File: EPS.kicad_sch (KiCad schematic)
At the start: 30 parts, among them SW101 Deploy_1, SW102 Deploy_2

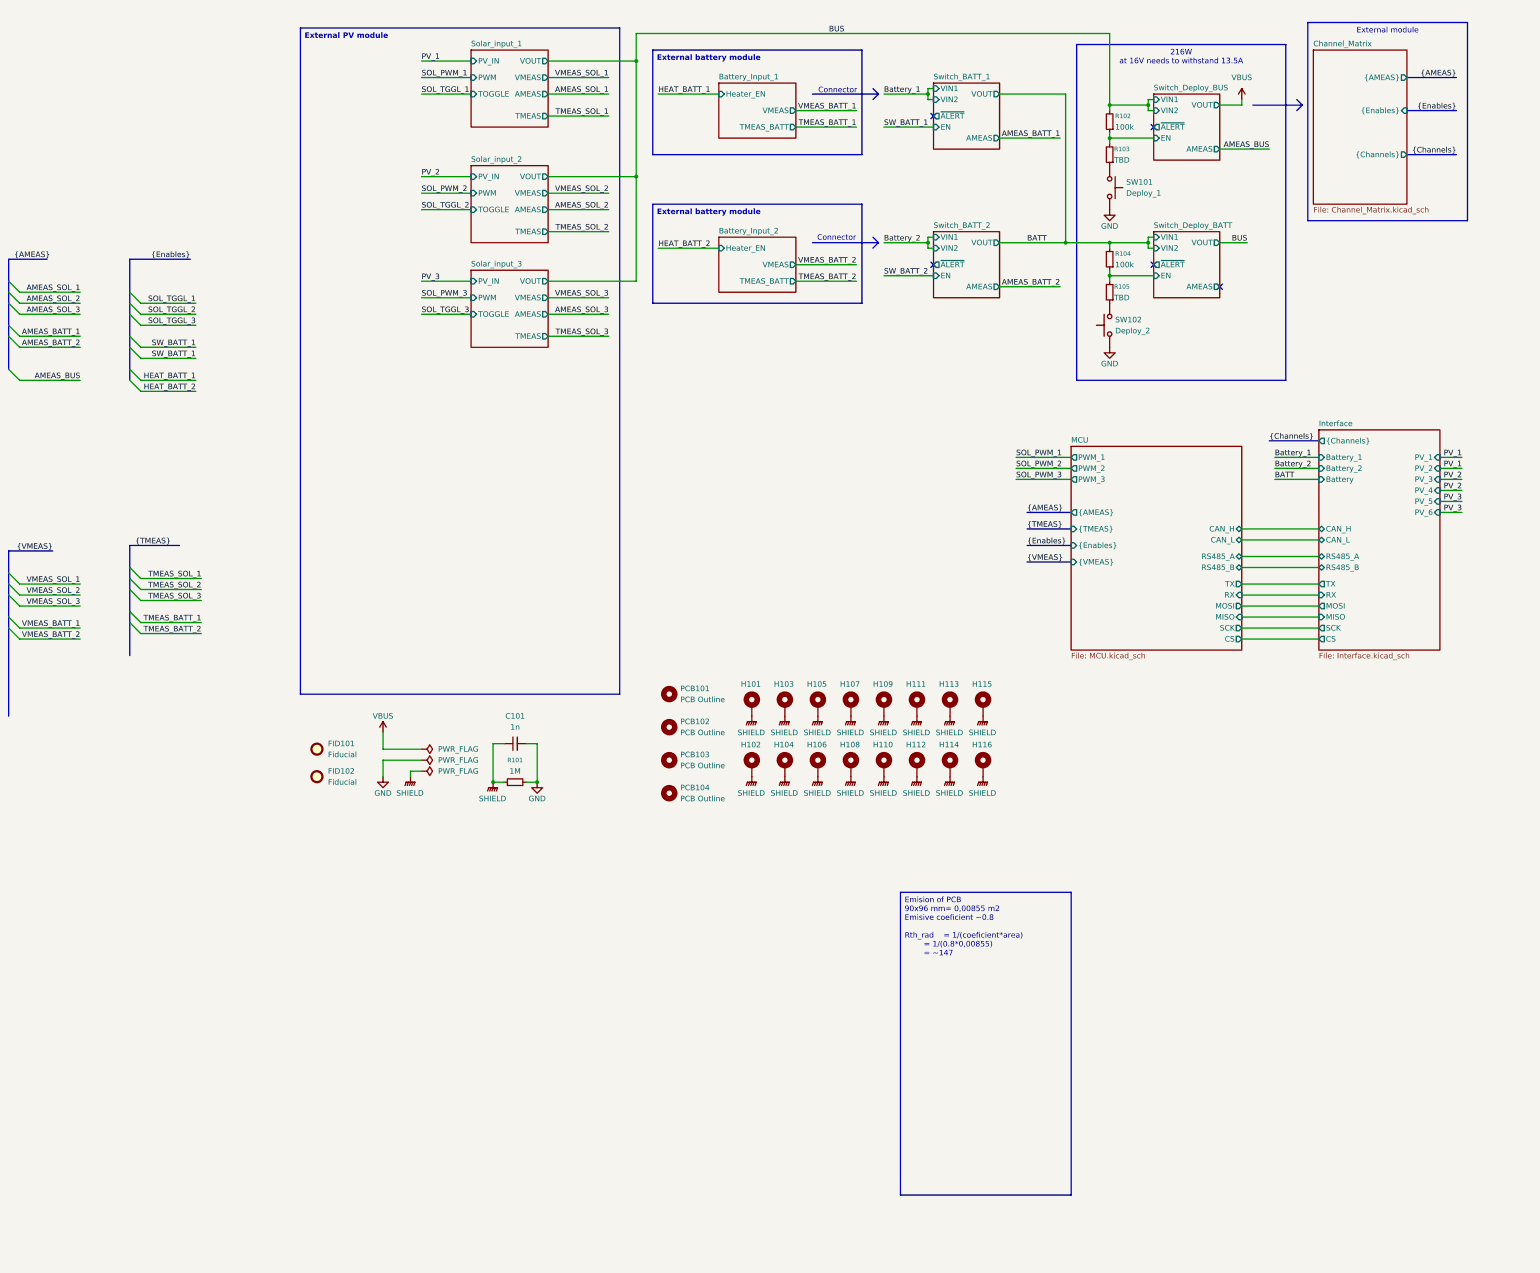
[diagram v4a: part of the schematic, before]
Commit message: connected CAN driver, added 3 solar inputs
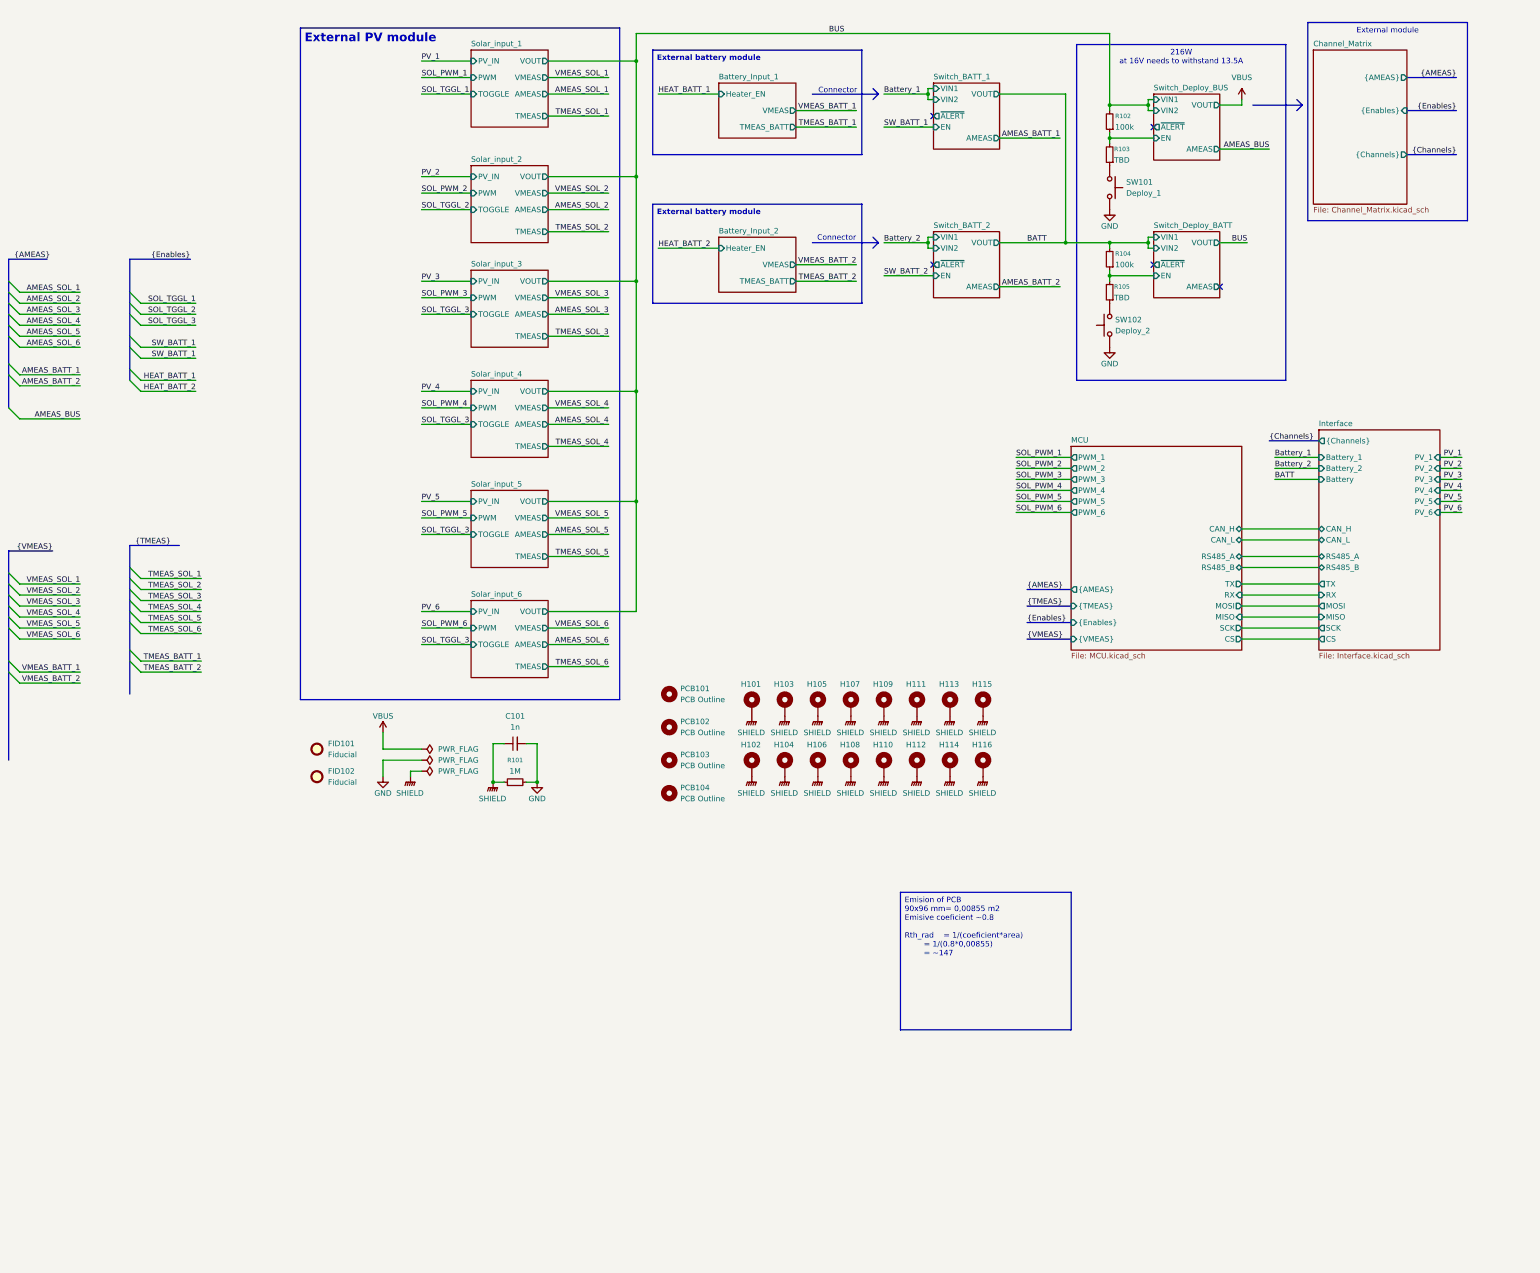
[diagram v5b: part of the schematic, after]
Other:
- added sheet Solar_input_4 (Solar_Cell_Input.kicad_sch)
- added sheet Solar_input_5 (Solar_Cell_Input.kicad_sch)
- added sheet Solar_input_6 (Solar_Cell_Input.kicad_sch)
- sheet MCU ports: added PWM_4, PWM_5, PWM_6; removed none

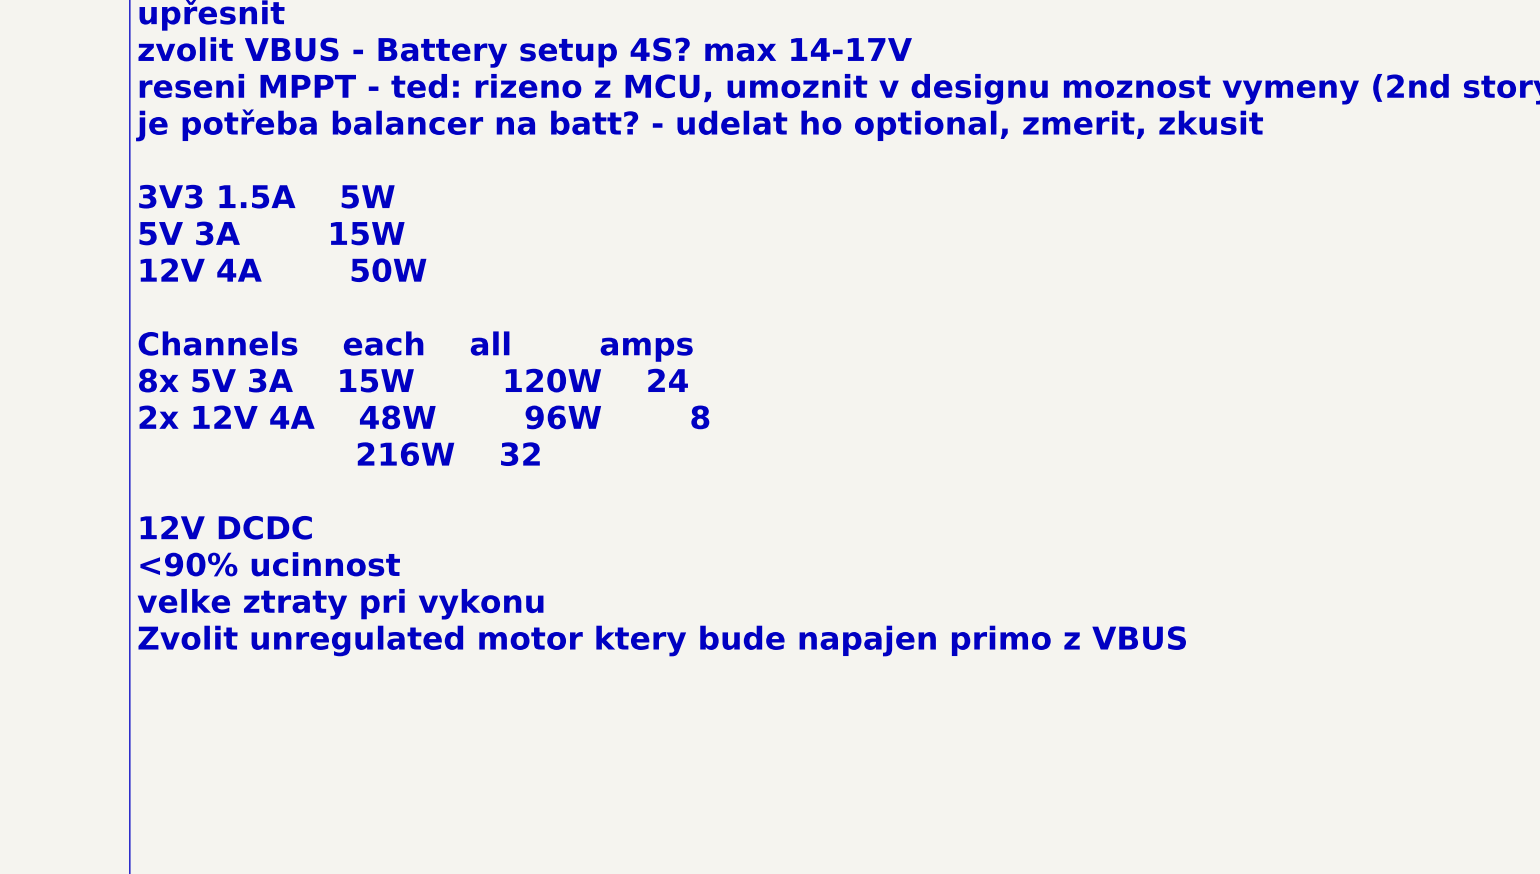
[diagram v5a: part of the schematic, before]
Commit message: added possible solutions for mppt
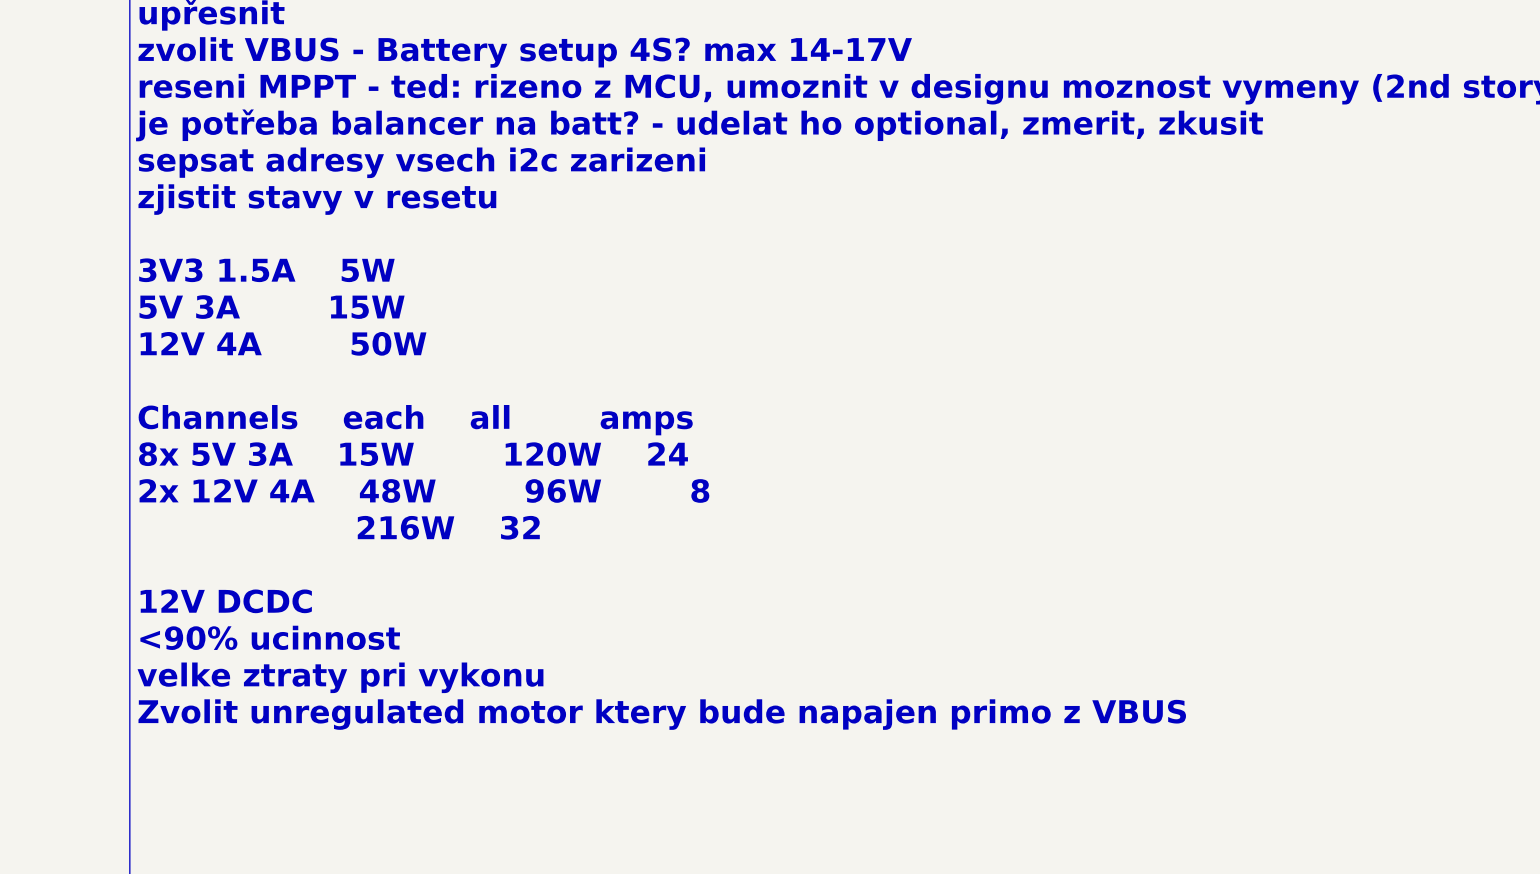
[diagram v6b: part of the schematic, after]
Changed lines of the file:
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@@
 		)
 	)
-	(text_box "upřesnit\nzvolit VBUS - Battery setup 4S? max 14-17V\nreseni MPPT - ted: rizeno z MCU, umoznit v designu moznost vymeny (2nd story nebo pajeny pcb modul)\nje potřeba balancer na batt? - udelat ho optional, zmerit, zkusit\n\n3V3 1.5A	5W\n5V 3A		15W\n12V 4A		50W\n\nChannels	each	all		amps\n8x 5V 3A	15W		120W	24\n2x 12V 4A	48W		96W		8\n					216W	32\n\n12V DCDC \n<90% ucinnost \nvelke ztraty pri vykonu\nZvolit unregulated motor ktery bude napajen primo z VBUS"
+	(text_box "upřesnit\nzvolit VBUS - Battery setup 4S? max 14-17V\nreseni MPPT - ted: rizeno z MCU, umoznit v designu moznost vymeny (2nd story nebo pajeny pcb modul)\nje potřeba balancer na batt? - udelat ho optional, zmerit, zkusit\nsepsat adresy vsech i2c zarizeni\nzjistit stavy v resetu\n\n3V3 1.5A	5W\n5V 3A		15W\n12V 4A		50W\n\nChannels	each	all		amps\n8x 5V 3A	15W		120W	24\n2x 12V 4A	48W		96W		8\n					216W	32\n\n12V DCDC \n<90% ucinnost \nvelke ztraty pri vykonu\nZvolit unregulated motor ktery bude napajen primo z VBUS"
 		(exclude_from_sim no)
 		(at 309.372 11.176 0)

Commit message: changed IO epanders to 2nd MSP430
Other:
- moved on the sheet: C101, FID101, FID102, H101, H102, H103, H104, H105, H106, H107, H108, H109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

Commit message: added RS422, housekeeping
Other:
- sheet Interface ports: added RS422_Rx_N, RS422_Rx_P, RS422_Tx_N, RS422_Tx_P; removed RS485_A, RS485_B
- sheet MCU ports: added RS422_Rx_N, RS422_Rx_P, RS422_Tx_N, RS422_Tx_P; removed PWM_1, PWM_2, PWM_3, PWM_4, PWM_5, PWM_6, RS485_A, RS485_B
- sheet Solar_input_1 ports: added none; removed PWM
- sheet Solar_input_2 ports: added none; removed PWM
- sheet Solar_input_3 ports: added none; removed PWM
- sheet Solar_input_4 ports: added none; removed PWM
- sheet Solar_input_5 ports: added none; removed PWM
- sheet Solar_input_6 ports: added none; removed PWM
- note added: "BATT CONN"
- note added: "Battery 1"
- note added: "Battery 2"
- note added: "DCDC MODE"
- note added: "HEAT EN"
- note added: "MAIN SWITCH"
- note added: "MEAS"
- note added: "Main PCB"
- note added: "OUTPUT PCB"
- note added: "PV input PCB"
- note added: "TMEAS"
- note added: "VBUS CONN"
